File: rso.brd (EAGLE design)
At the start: 160 x 100 mm, 24 parts, among them X10 1-227161-0, X6 1-227161-0, X7 1-227161-0, X8 1-227161-0, X9 1-227161-0

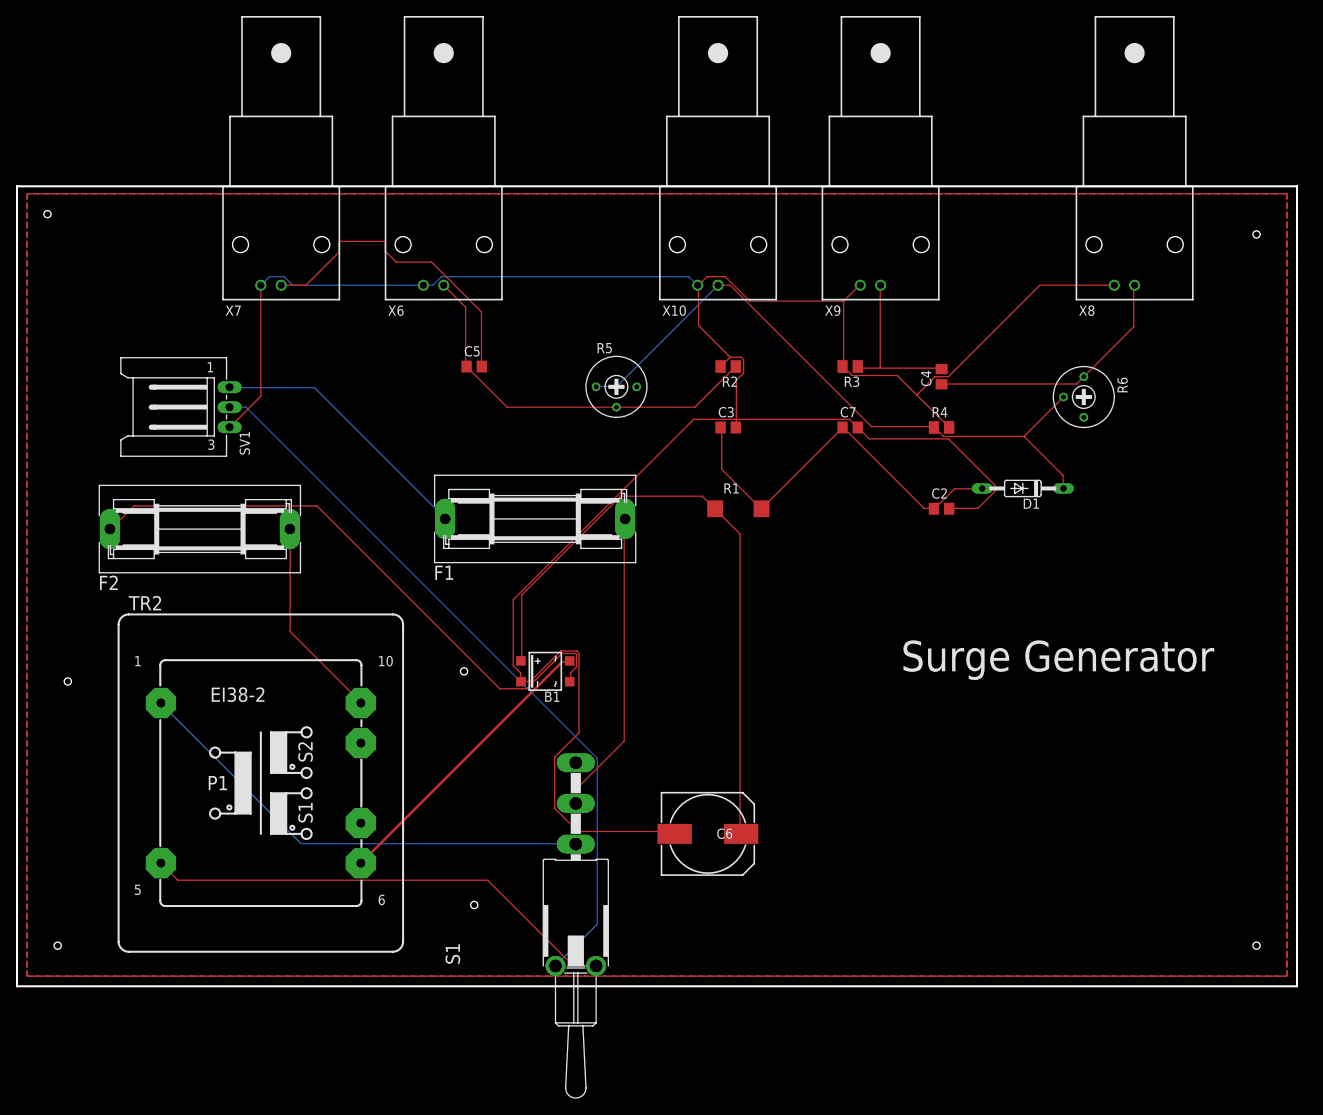
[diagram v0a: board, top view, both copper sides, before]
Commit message: CHanges to the thikness of the tracks
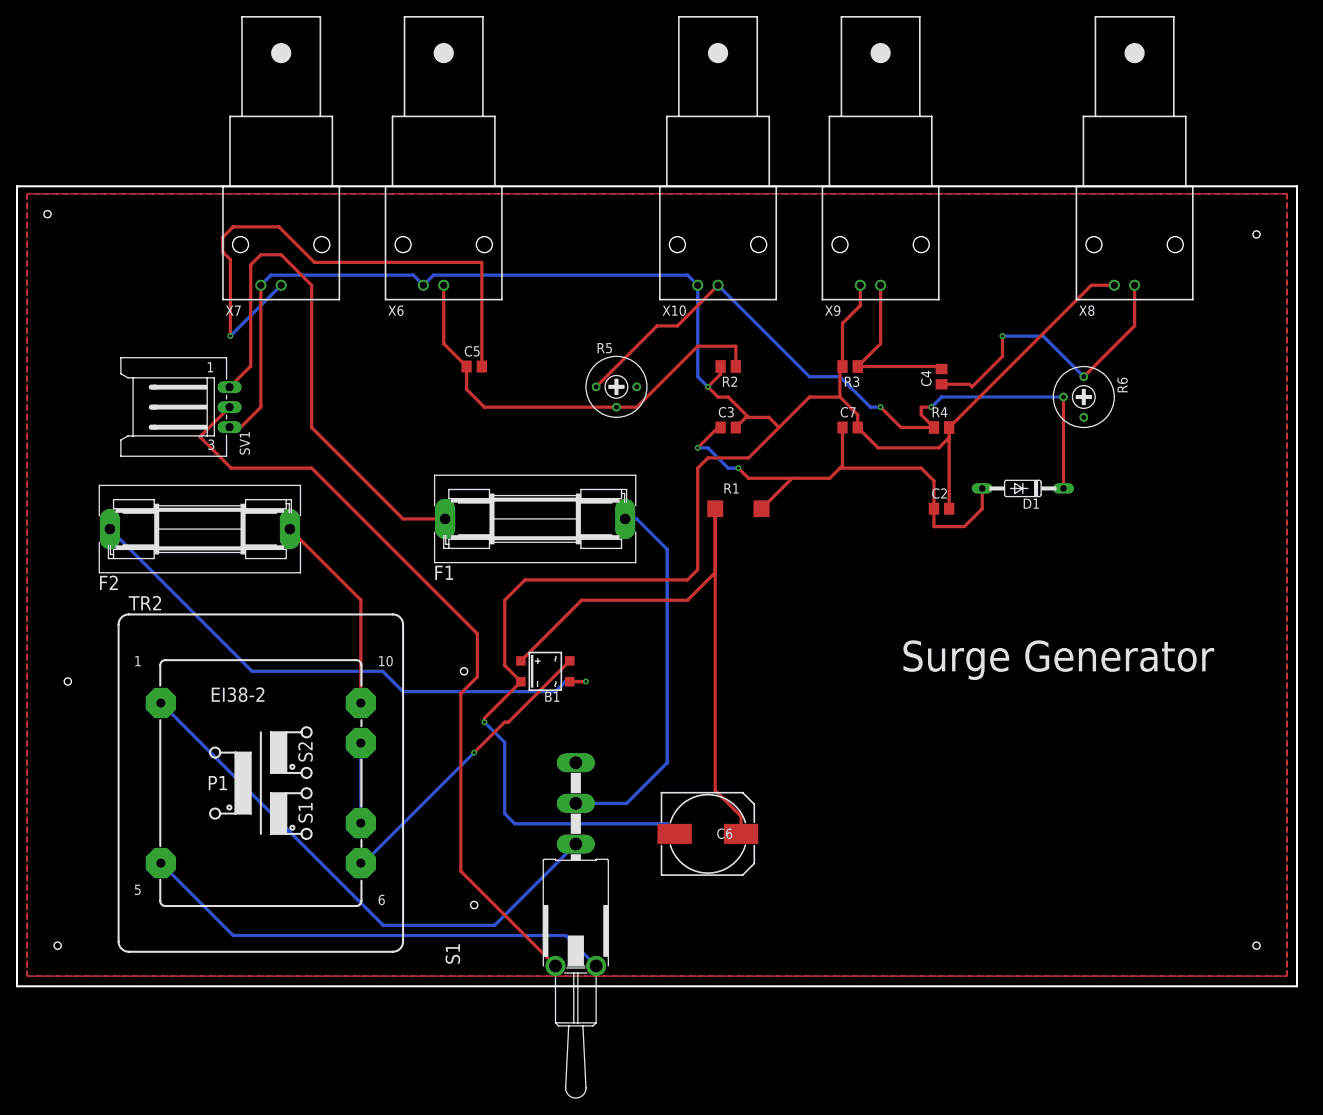
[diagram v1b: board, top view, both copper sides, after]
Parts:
- D1: value (none) -> none
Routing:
- net N$5: track 33.8 -> 65.3 mm
- net N$15: track 39.0 -> 69.5 mm, vias 0 -> 1
- net GND: track 313.6 -> 290.4 mm, vias 0 -> 2
- net N$11: track 49.4 -> 62.0 mm, vias 0 -> 2
- net N$6: track 38.2 -> 47.0 mm
- net N$8: track 59.2 -> 67.6 mm
- net N$13: track 32.3 -> 38.2 mm, vias 0 -> 1
- net N$12: track 82.1 -> 87.8 mm, vias 0 -> 2
- net N$14: track 49.2 -> 54.5 mm
- net N$4: track 92.3 -> 97.4 mm
- net N$1: track 74.7 -> 70.5 mm, vias 0 -> 1
- net N$9: track 80.3 -> 78.8 mm
- net N$10: track 21.1 -> 22.0 mm
- net N$2: vias 0 -> 1
